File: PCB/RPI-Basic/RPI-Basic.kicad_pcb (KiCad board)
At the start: 2 copper layers, 90 x 90 mm, 3 parts, among them J1 SE2-30, J2 Conn_02x20_Odd_Even, J3 Conn_02x20_Odd_Even

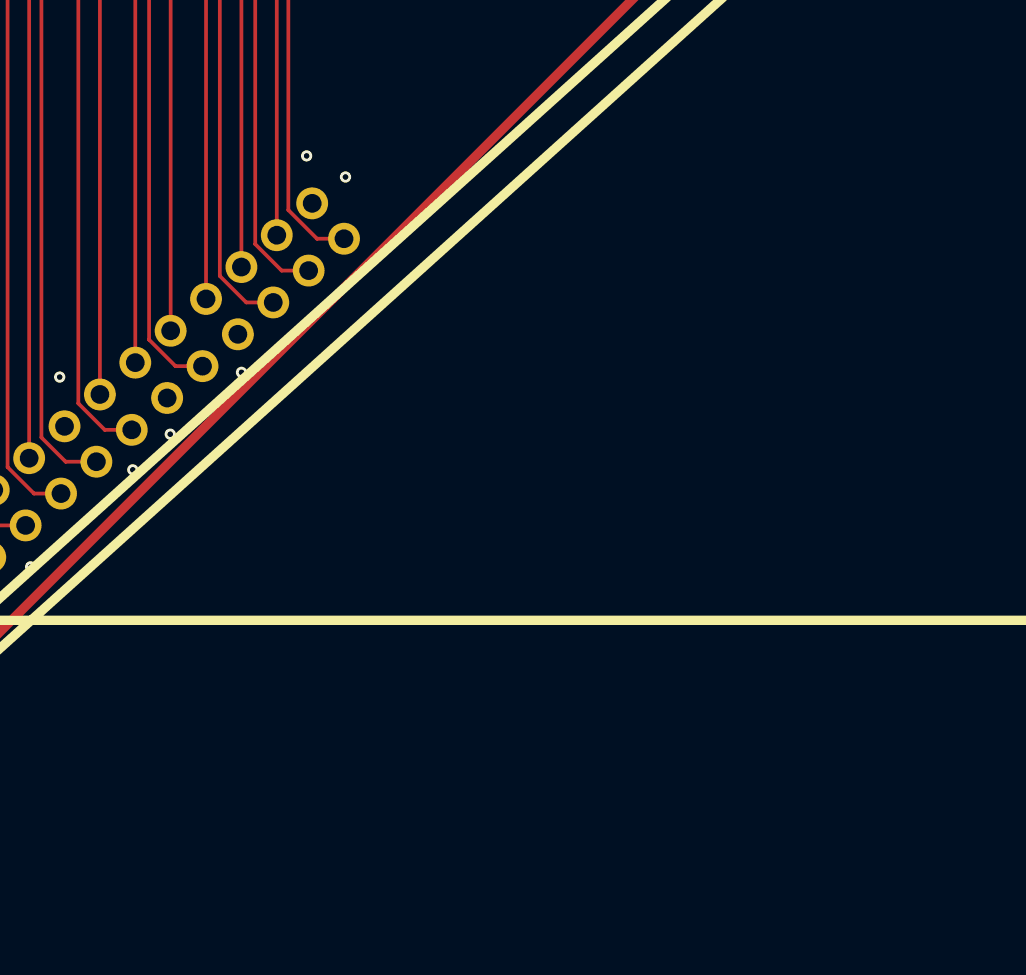
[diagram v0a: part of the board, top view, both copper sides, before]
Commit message: added support mounting
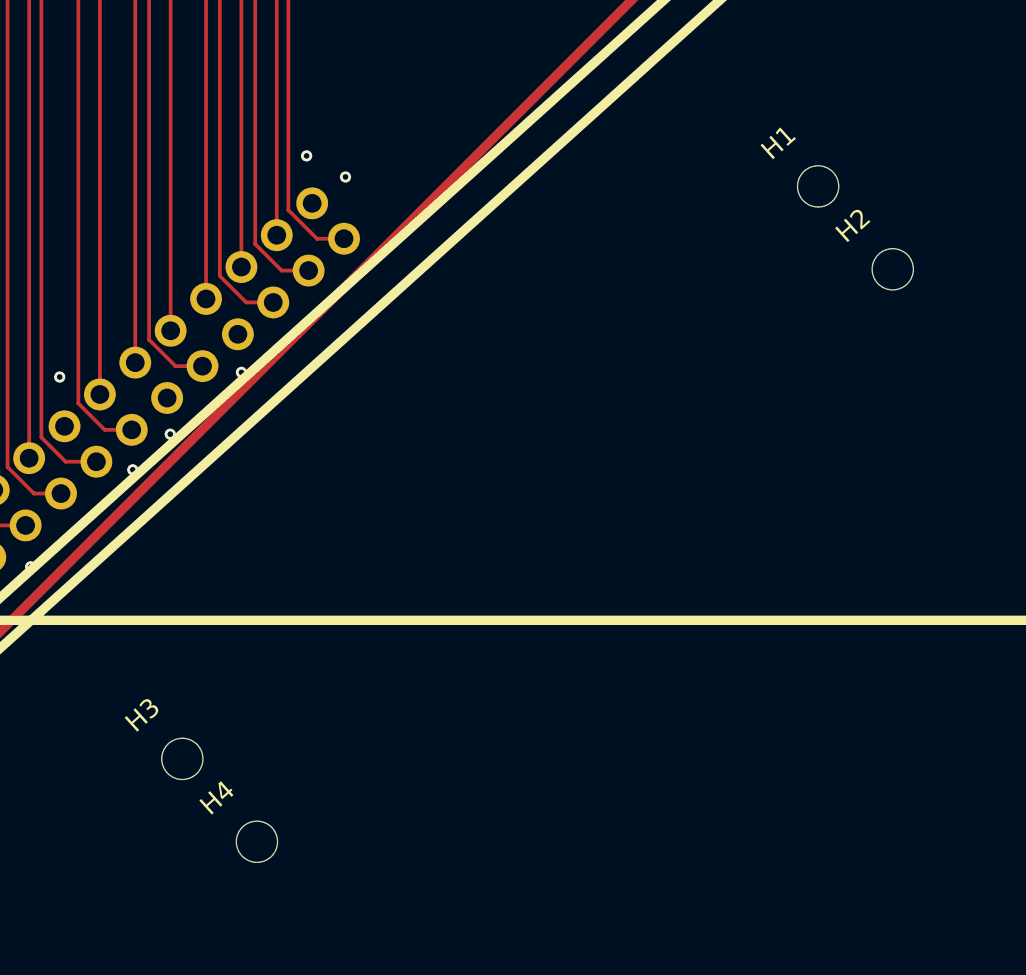
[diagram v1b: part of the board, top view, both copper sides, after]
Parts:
- added H1: MountingHole, MountingHole:MountingHole_2.2mm_M2, F.Cu at (166.3, 86.8)
- added H2: MountingHole, MountingHole:MountingHole_2.2mm_M2, F.Cu at (170.3, 91.2)
- added H3: MountingHole, MountingHole:MountingHole_2.2mm_M2, F.Cu at (132.4, 117.4)
- added H4: MountingHole, MountingHole:MountingHole_2.2mm_M2, F.Cu at (136.4, 121.8)

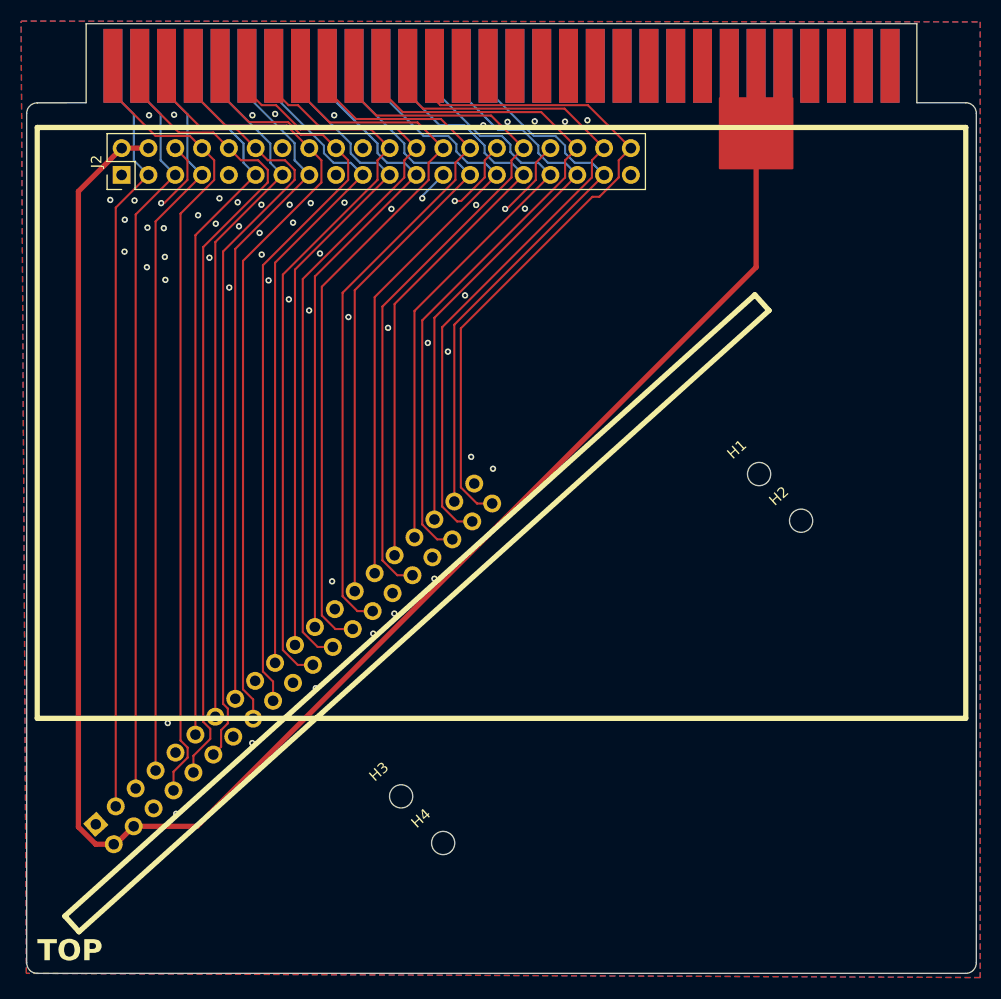
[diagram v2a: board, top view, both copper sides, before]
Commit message: updated board footprint and rerouted
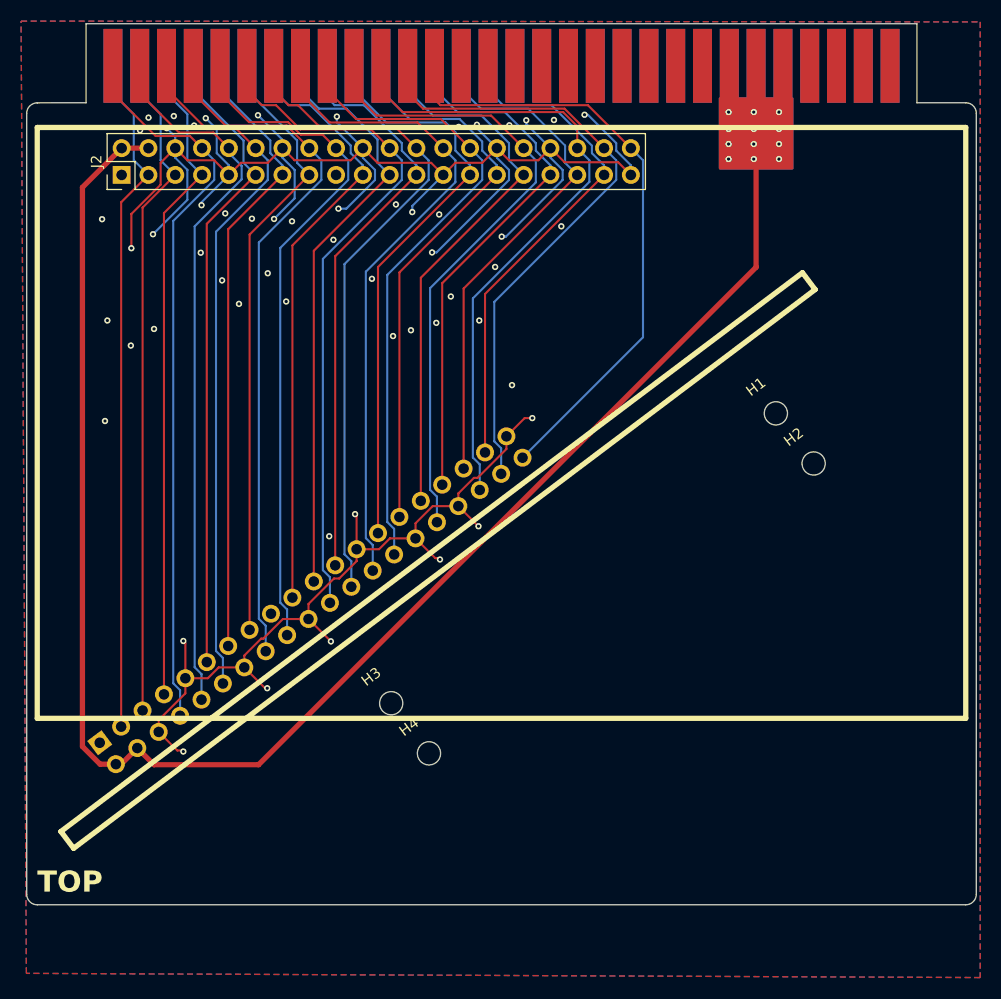
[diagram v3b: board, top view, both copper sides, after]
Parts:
- moved H3 8.88 mm to (131.4, 108.5), turned to 37 degrees
- moved H4 8.60 mm to (135.0, 113.3), turned to 37 degrees
- moved J3 7.74 mm to (103.8, 112.3), turned to -53 degrees
- moved H1 5.97 mm to (167.9, 81.1), turned to 37 degrees
- moved H2 5.55 mm to (171.5, 85.8), turned to 37 degrees
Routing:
- net GND: track 24.6 -> 227.9 mm, vias 58 -> 56
- net /15: track 78.3 -> 68.1 mm
- net /18: track 76.7 -> 66.5 mm
- net +5V: track 171.4 -> 161.4 mm, vias 0 -> 12
- net /21: track 66.5 -> 58.2 mm
- net /25: track 73.3 -> 65.1 mm
- net /7: track 70.8 -> 62.6 mm
- net /8: track 71.9 -> 63.7 mm
- net /1: track 69.0 -> 61.1 mm
- net /2: track 72.9 -> 65.1 mm
- net /12: track 68.9 -> 61.2 mm
- net /3: track 71.4 -> 63.8 mm
- net /4: track 70.0 -> 62.5 mm
- net /20: track 67.1 -> 59.8 mm
- net /14: track 76.7 -> 69.4 mm
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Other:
- board size 90 x 90 mm -> 90 x 83.5 mm
